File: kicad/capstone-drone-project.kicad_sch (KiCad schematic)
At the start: 29 parts, among them Q1 PMOS, Q2 PMOS, Q3 NMOS, U1 ESP32-S3, Y1 ECS-400-10-37B2-CKY-TR

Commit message: updating text
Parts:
- removed C12: 10n, symbol Device:C
- C11: value 1u -> 0.1u
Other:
- note added: "-add uart and usb interface"
- note added: "-assume 5pF Cstray -Cl=10pF"
- note added: "-at least 50us for power rails to stabilize before CHIP_PU is pulled high -at least 50us for CHIP_PU to stay below Vil_nrst to reset chip"
- note removed: "10pF capacitors w/ 10pF oscillator, assuming 5pF stray capacitance; this is a wip - need to do more research"
- note removed: "may need to add RC delay circuit here to account for tstbl and trst tstbl - at least 50us for power rails to stabilize before CHIP_PU is pulled high trst - at least 50us for CHIP_PU to stay below Vil_nrst to reset chip"
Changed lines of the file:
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@@
 		)
 	)
-	(text "10pF capacitors w/ 10pF oscillator, assuming 5pF stray capacitance; this is a wip - need to do more research"
+	(text "-assume 5pF Cstray\n-Cl=10pF"
 		(exclude_from_sim no)
-		(at 99.314 146.304 0)
+		(at 100.584 133.604 0)
 		(effects
 			(font
@@
 		)
 	)
-	(text "may need to add RC delay circuit here to account for tstbl and trst\ntstbl - at least 50us for power rails to stabilize before CHIP_PU is pulled high\ntrst - at least 50us for CHIP_PU to stay below Vil_nrst to reset chip"
+	(text "-add uart and usb interface"
 		(exclude_from_sim no)
-		(at 230.886 101.6 0)
+		(at 238.506 86.36 0)
+		(effects
+			(font
+				(size 1.27 1.27)
+			)
+		)
+	)
+	(text "-at least 50us for power rails to stabilize before CHIP_PU is pulled high\n-at least 50us for CHIP_PU to stay below Vil_nrst to reset chip"
+		(exclude_from_sim no)
+		(at 205.486 137.16 0)
 		(effects
 			(font
@@
 	)
 	(junction
-		(at 33.02 93.98)
-		(diameter 0)
-		(color 0 0 0 0)
-	)
-	(junction
 		(at 25.4 74.93)
 		(diameter 0)
@@
 	(wire
 		(pts
-			(xy 33.02 93.98) (xy 43.18 93.98)
-		)
-		(stroke
-			(width 0)
-			(type default)
-		)
-	)
-	(wire
-		(pts
 			(xy 135.89 29.21) (xy 135.89 30.48)
 		)
@@
 			)
 		)
-		(property "Value" "1u"
+		(property "Value" "0.1u"
 			(at 36.83 99.0599 0)
 			(effects
@@
 	)
 	(symbol
-		(lib_id "power:GND")
-		(at 43.18 101.6 0)
-		(unit 1)
-		(exclude_from_sim no)
-		(in_bom yes)
-		(on_board yes)
-		(dnp no)
-		(fields_autoplaced yes)
-		(property "Reference" "#PWR017"
-			(at 43.18 107.95 0)
-			(effects
-				(font
-					(size 1.27 1.27)
-				)
-				(hide yes)
-			)
-		)
-		(property "Value" "GND"
-			(at 43.18 106.68 0)
-			(effects
-				(font
-					(size 1.27 1.27)
-				)
-			)
-		)
-		(property "Footprint" ""
-			(at 43.18 101.6 0)
-			(effects
-				(font
-					(size 1.27 1.27)
-				)
-				(hide yes)
-			)
-		)
-		(property "Datasheet" ""
-			(at 43.18 101.6 0)
-			(effects
-				(font
-					(size 1.27 1.27)
-				)
-				(hide yes)
-			)
-		)
-		(property "Description" "Power symbol creates a global label with name \"GND\" , ground"
-			(at 43.18 101.6 0)
-			(effects
-				(font
-					(size 1.27 1.27)
-				)
-				(hide yes)
-			)
-		)
-		(pin "1"
-		)
-		(instances
-			(project "capstone-drone-project"
-				(path "/99584293-ff2b-4397-8b8b-c39f1581dc82"
-					(reference "#PWR017")
-					(unit 1)
-				)
-			)
-		)
-	)
-	(symbol
 		(lib_id "Device:C")
 		(at 237.49 40.64 0)
@@
 					(unit 1)
 				)
-			)
-		)
-	)
-	(symbol
-		(lib_id "Device:C")
-		(at 43.18 97.79 0)
-		(unit 1)
-		(exclude_from_sim no)
-		(in_bom yes)
-		(on_board yes)
-		(dnp no)
-		(fields_autoplaced yes)
-		(property "Reference" "C12"
-			(at 46.99 96.5199 0)
-			(effects
-				(font
-					(size 1.27 1.27)
-				)
-				(justify left)
-			)
-		)
-		(property "Value" "10n"
-			(at 46.99 99.0599 0)
-			(effects
-				(font
-					(size 1.27 1.27)
-				)
-				(justify left)
-			)
-		)
-		(property "Footprint" ""
-			(at 44.1452 101.6 0)
-			(effects
-				(font
-					(size 1.27 1.27)
-				)
-				(hide yes)
-			)
-		)
-		(property "Datasheet" "~"
-			(at 43.18 97.79 0)
-			(effects
-				(font
-					(size 1.27 1.27)
-				)
-				(hide yes)
-			)
-		)
-		(property "Description" "Unpolarized capacitor"
-			(at 43.18 97.79 0)
-			(effects
-				(font
-					(size 1.27 1.27)
-				)
-				(hide yes)
-			)
-		)
-		(pin "1"
-		)
-		(pin "2"
-		)
-		(instances
-			(project "capstone-drone-project"
-				(path "/99584293-ff2b-4397-8b8b-c39f1581dc82"
-					(reference "C12")
-					(unit 1)
-				)

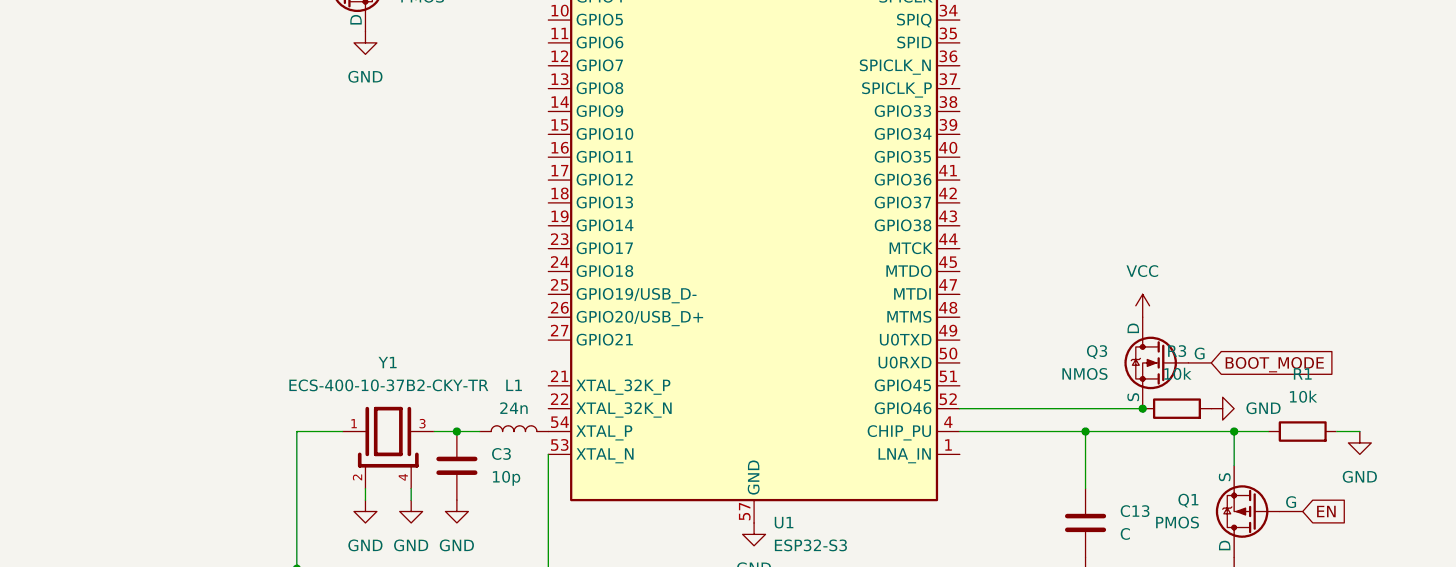
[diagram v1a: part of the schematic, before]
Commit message: add uart
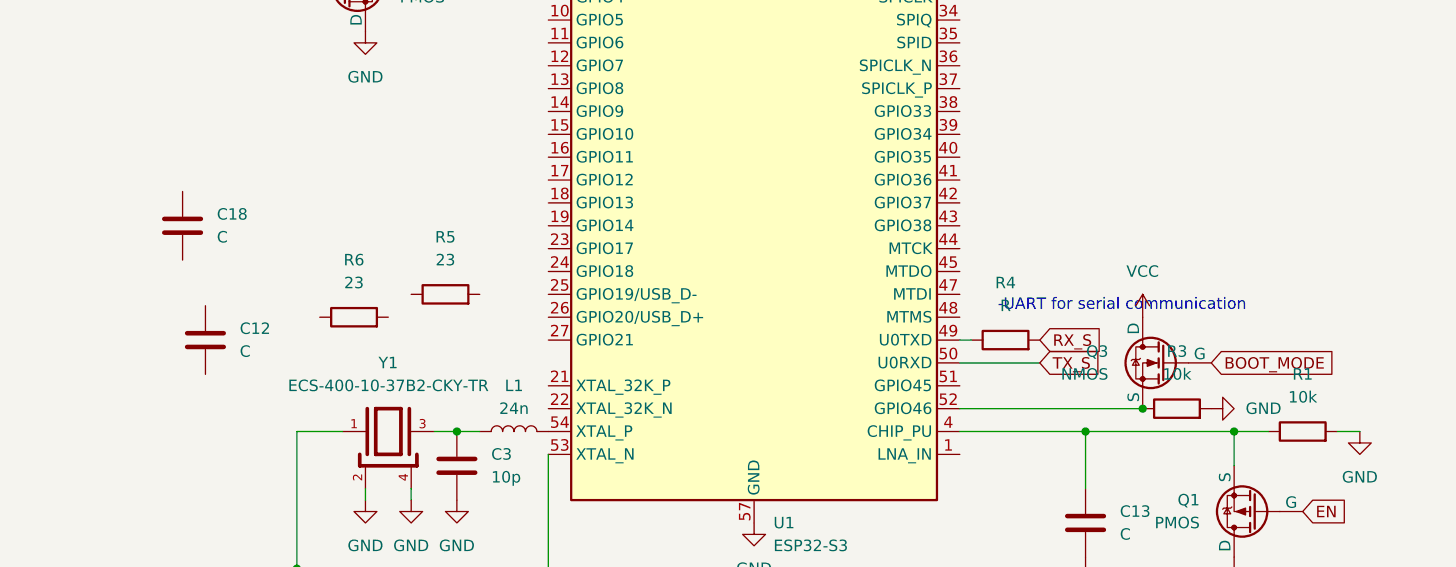
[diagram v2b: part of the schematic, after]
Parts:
- added C12, C18: C, symbol Device:C
- added R4: R, symbol Device:R
- added R5, R6: 23, symbol Device:R
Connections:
- net at U1.49 (U0TXD): now also R4.1
- net TX_S: now reaches U1.50 (U0RXD)
- new net RX_S: R4.2
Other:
- note added: "-UART for serial communication"

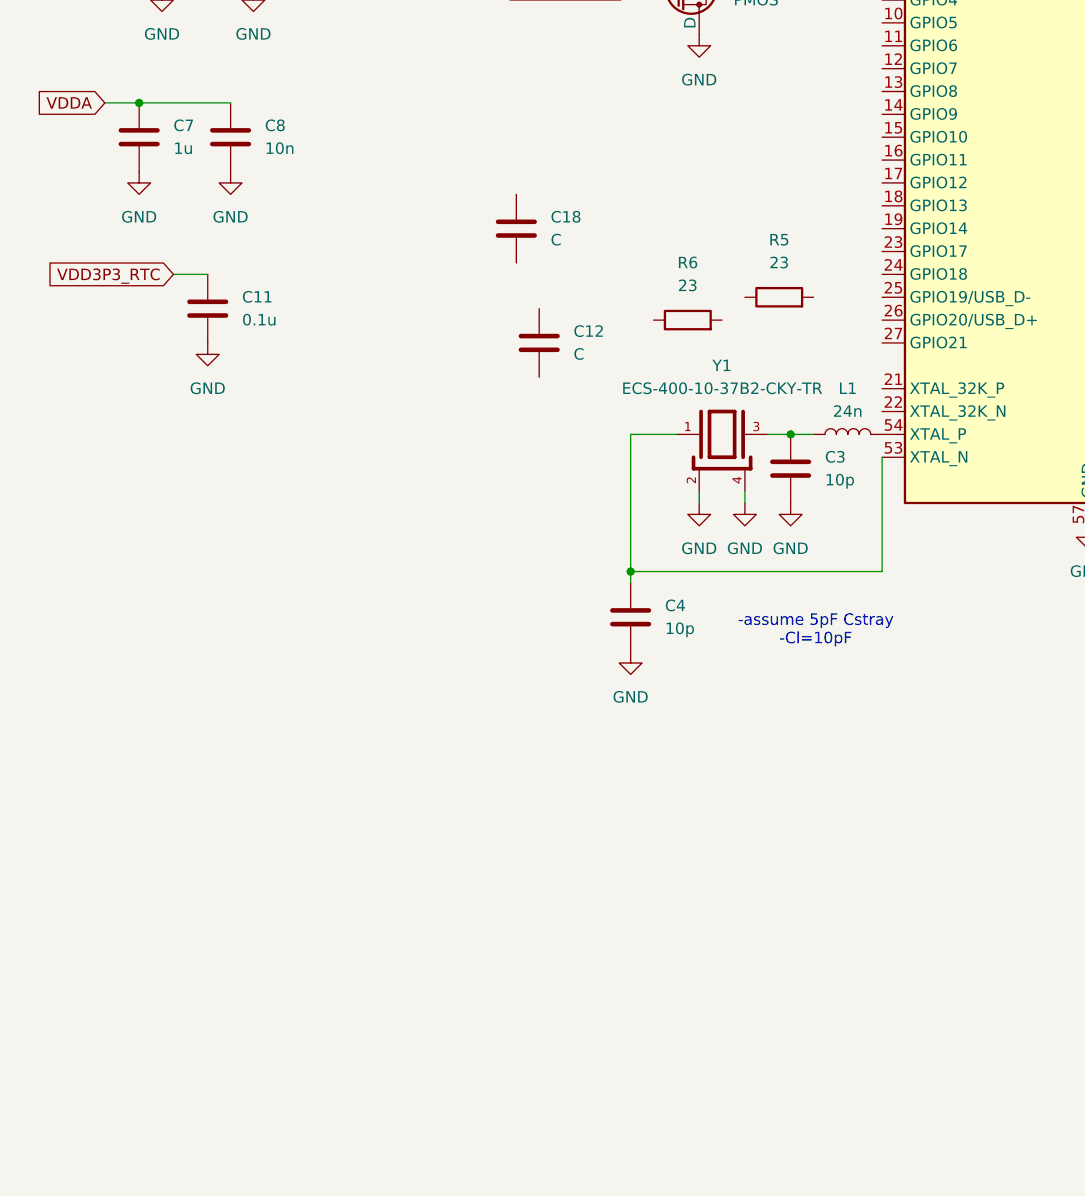
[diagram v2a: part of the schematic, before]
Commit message: add basic usb interface
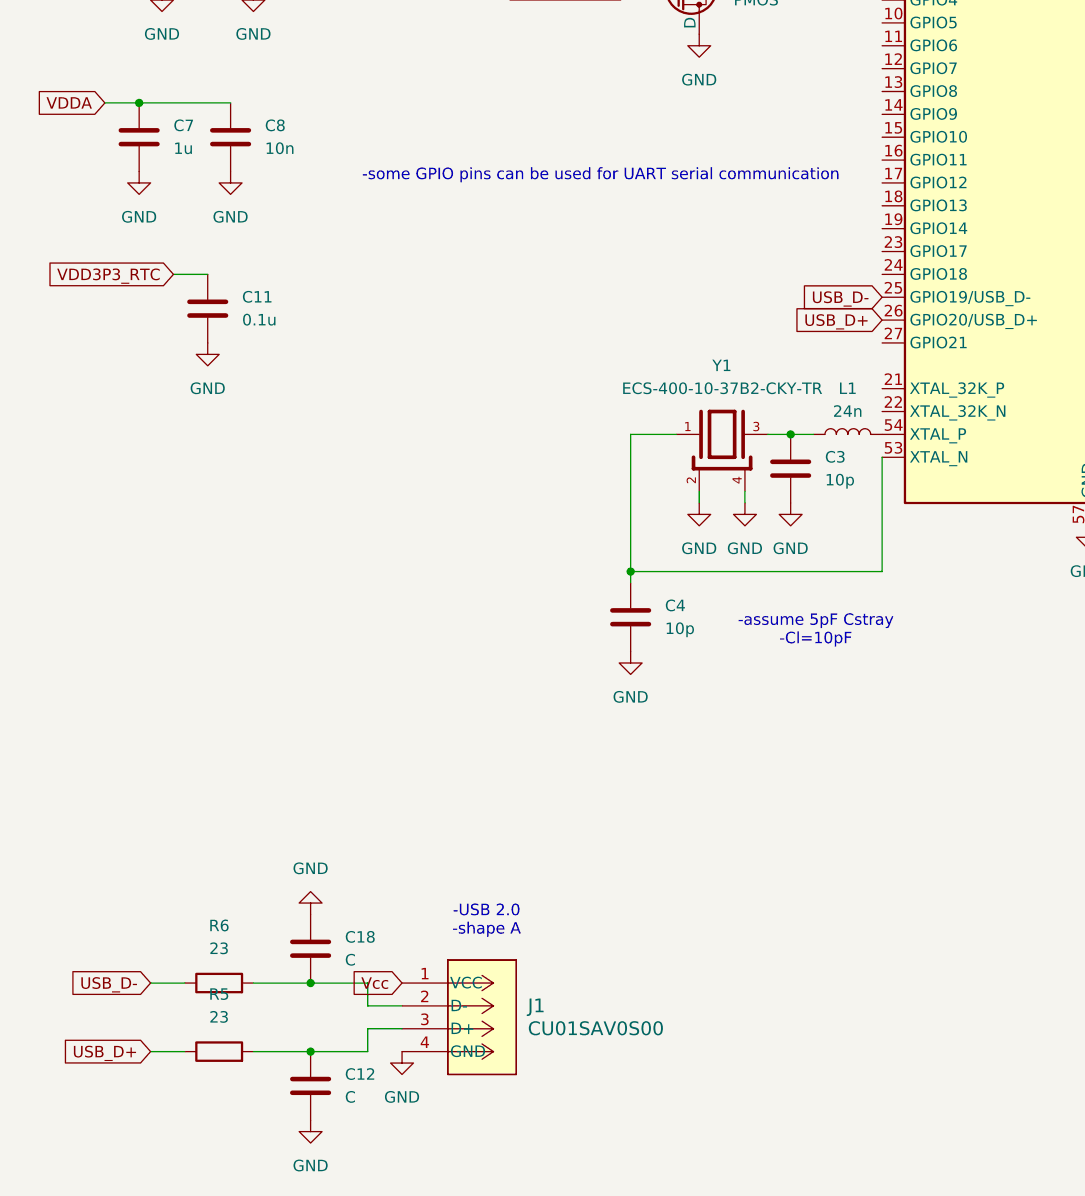
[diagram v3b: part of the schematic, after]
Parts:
- added J1: CU01SAV0S00, CONN_CU01SAV_CVI, symbol 2025-09-29_15-54-09:CU01SAV0S00
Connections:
- net GND: now also C12.2, C18.1, J1.4 (GND)
- net VDD3P3: now also J1.1 (VCC)
- net USB_D-: now reaches U1.25 (GPIO19/USB_D-)
- net USB_D-: now also R6.1
- net USB_D+: now reaches U1.26 (GPIO20/USB_D+)
- net USB_D+: now also R5.1
- net at R6.2: now also C18.2, J1.2 (D-)
- net at C12.1: now also R5.2, J1.3 (D+)
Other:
- note added: "-USB 2.0 -shape A"
- note added: "-some GPIO pins can be used for UART serial communication"
- moved on the sheet: C12, C18, R6

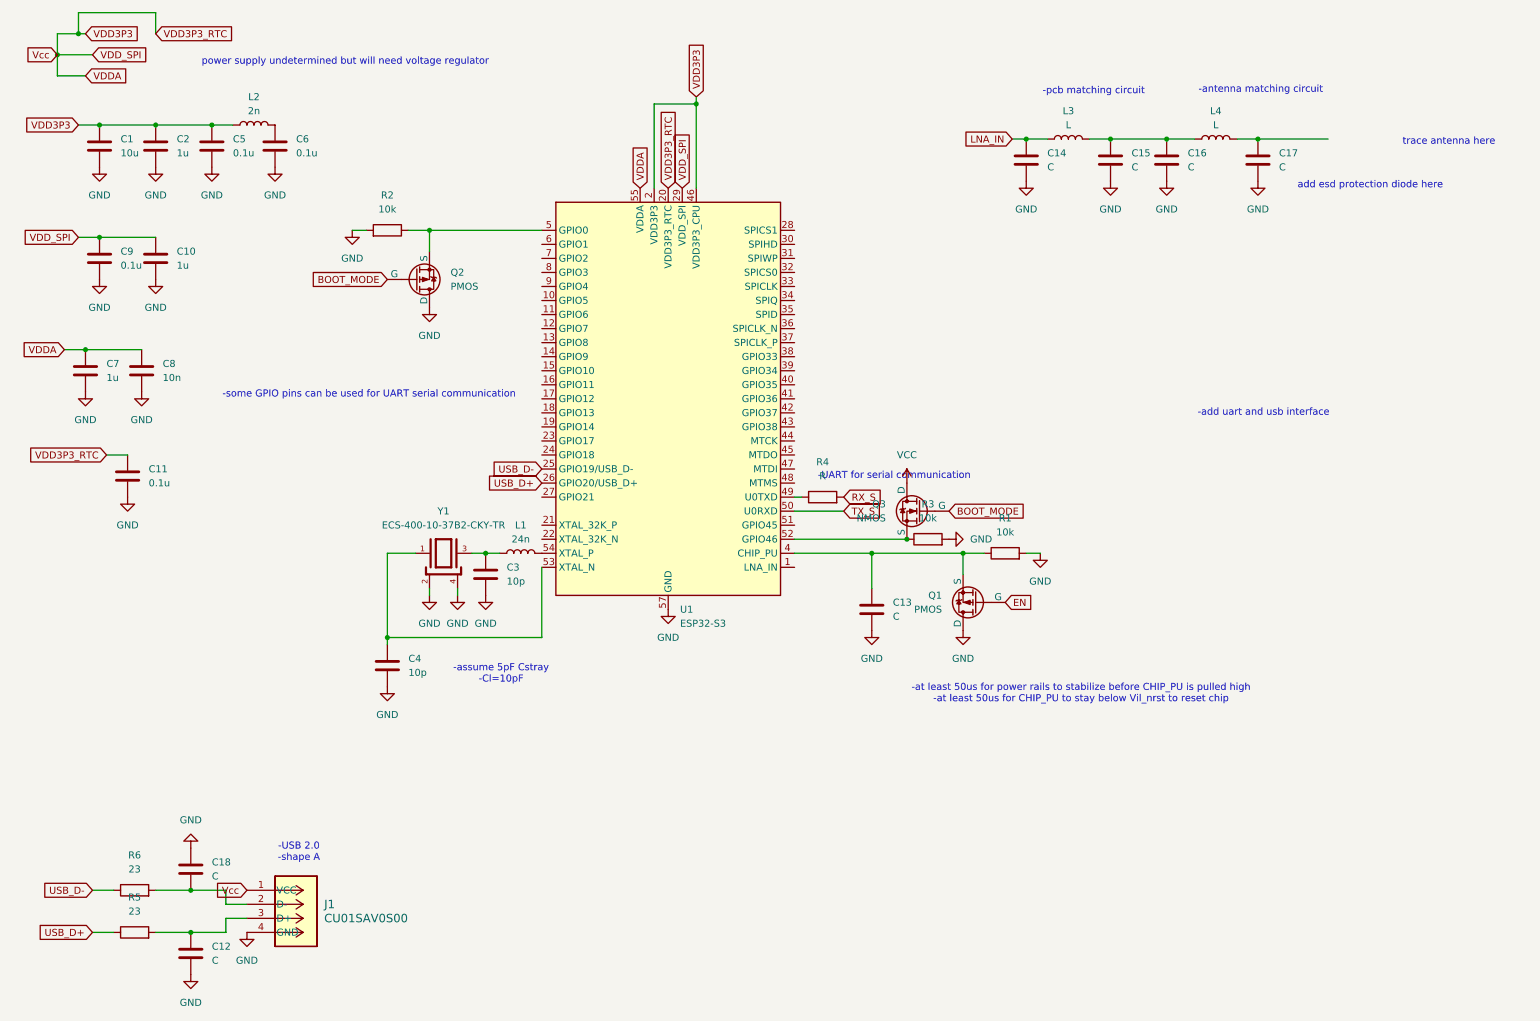
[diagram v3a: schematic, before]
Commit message: add lost parts
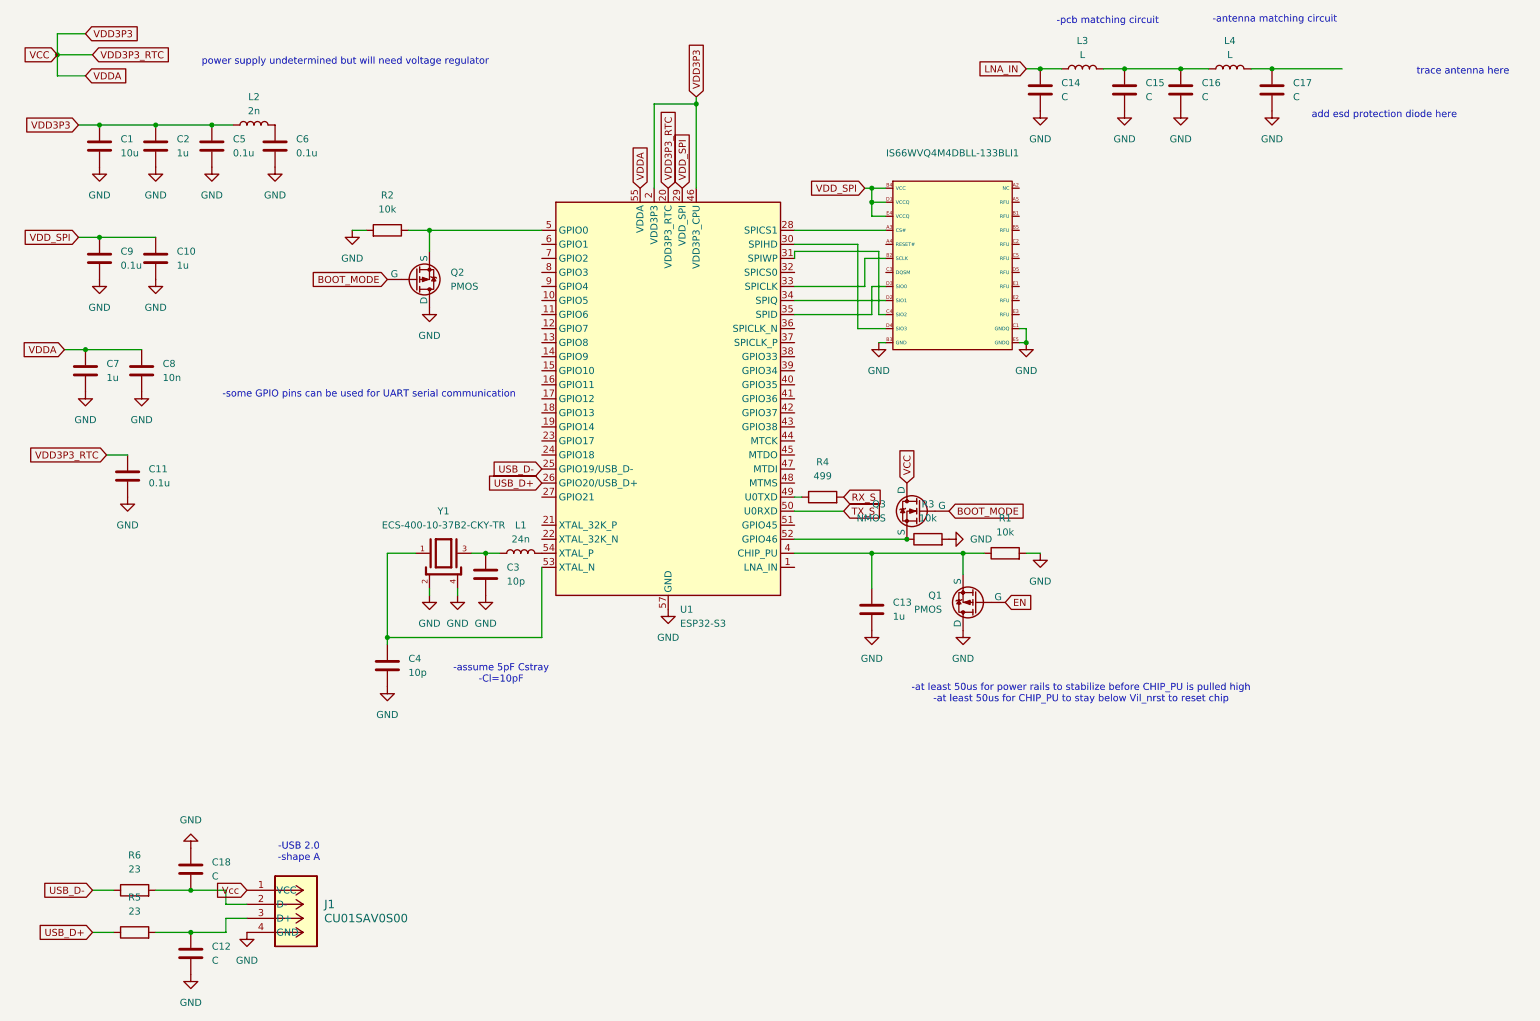
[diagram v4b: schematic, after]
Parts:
- added IS66WVQ4M4DBLL-133BLI1: ~, symbol capstone-drone-project-custom-symbols:IS66WVQ4M4DBLL-133BLI
- C13: value C -> 1u
- R4: value R -> 499
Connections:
- net GND: now also IS66WVQ4M4DBLL-133BLI1.B3 (GND), IS66WVQ4M4DBLL-133BLI1.C1 (GNDQ), IS66WVQ4M4DBLL-133BLI1.E5 (GNDQ)
- net VCC: now also C1.1, C11.1, C2.1, C5.1, C7.1, C8.1, L2.1, U1.2 (VDD3P3), U1.20 (VDD3P3_RTC), U1.3 (VDD3P3), U1.46 (VDD3P3_CPU), U1.55 (VDDA), U1.56 (VDDA)
- net at U1.28 (SPICS1): now also IS66WVQ4M4DBLL-133BLI1.A3 (CS#)
- net at U1.30 (SPIHD): now also IS66WVQ4M4DBLL-133BLI1.D4 (SIO3)
- net at U1.31 (SPIWP): now also IS66WVQ4M4DBLL-133BLI1.C4 (SIO2)
- net at U1.33 (SPICLK): now also IS66WVQ4M4DBLL-133BLI1.B2 (SCLK)
- net at U1.34 (SPIQ): now also IS66WVQ4M4DBLL-133BLI1.D2 (SIO1)
- net at U1.35 (SPID): now also IS66WVQ4M4DBLL-133BLI1.D3 (SIO0)
- removed net VDD3P3: C1.1, C10.1, C11.1, C2.1, C5.1, C7.1, C8.1, C9.1, J1.1 (VCC), L2.1, U1.2 (VDD3P3), U1.20 (VDD3P3_RTC), U1.29 (VDD_SPI), U1.3 (VDD3P3), U1.46 (VDD3P3_CPU), U1.55 (VDDA), U1.56 (VDDA)
- new net VDD_SPI: C10.1, C9.1, IS66WVQ4M4DBLL-133BLI1.B4 (VCC), IS66WVQ4M4DBLL-133BLI1.D1 (VCCQ), IS66WVQ4M4DBLL-133BLI1.E4 (VCCQ), U1.29 (VDD_SPI)
- new net Vcc: J1.1 (VCC)
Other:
- note removed: "-UART for serial communication"
- note removed: "-add uart and usb interface"
- moved on the sheet: C14, C15, C16, C17, L3, L4
